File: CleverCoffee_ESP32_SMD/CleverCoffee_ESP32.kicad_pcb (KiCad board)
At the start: 2 copper layers, 51.5 x 81.8 mm, 48 parts, among them Q1 2N7002, Q2 2N7002, Q3 2N7002, Q4 2N7002, Q5 2N7002

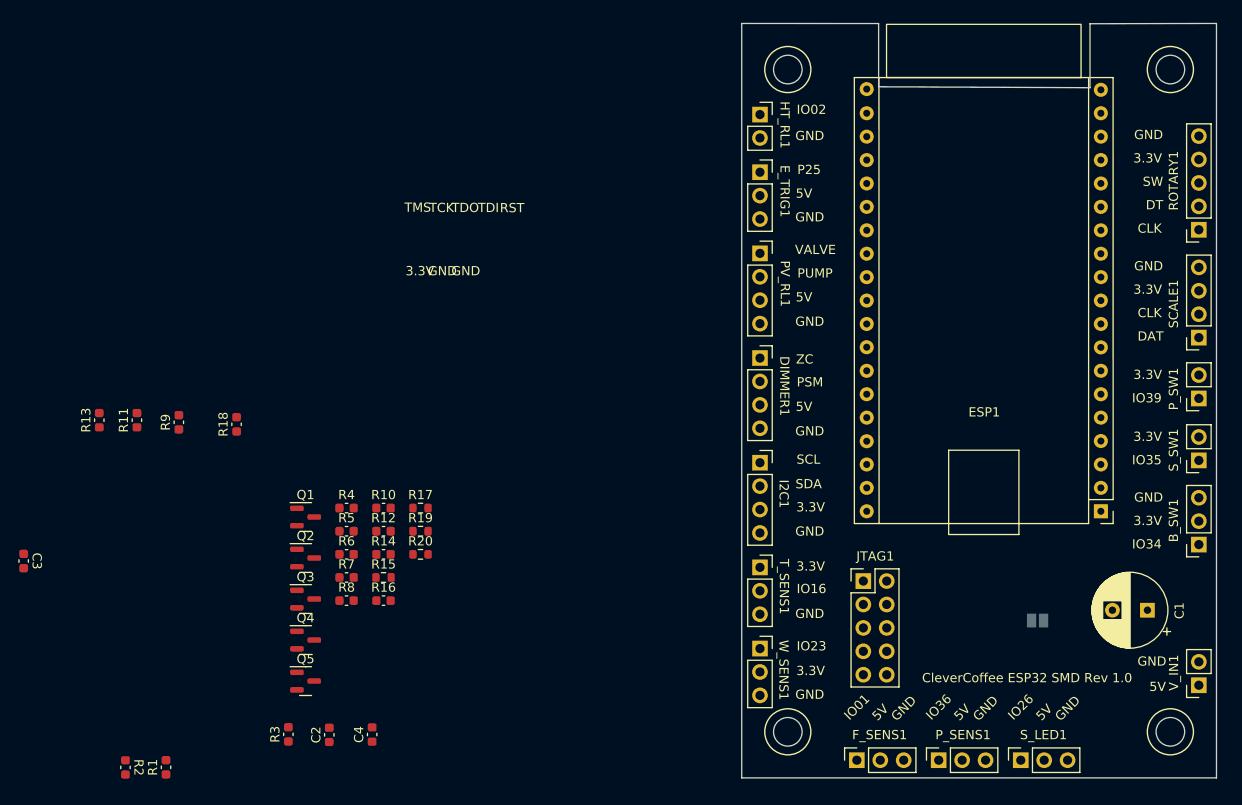
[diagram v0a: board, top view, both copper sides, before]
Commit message: Finishes SMD version for production
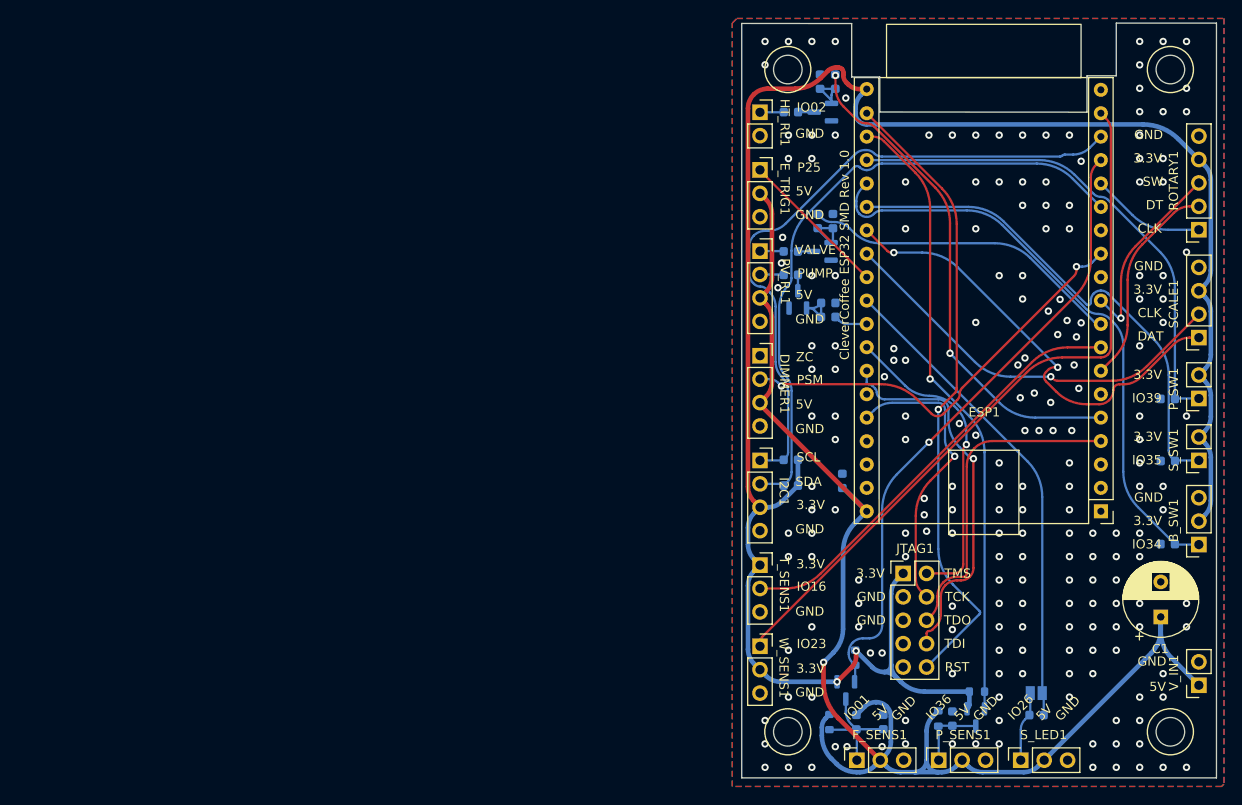
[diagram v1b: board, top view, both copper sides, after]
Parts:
- C2, C3, C4, Q1, Q2, Q3, Q4, Q5, R1, R10, R11, R12, R13, R14, R15, R16, R17, R18, R19, R2, R20, R3, R4, R5, R6, R7, R8, R9: moved to B.Cu
- moved R13 115.9 mm to (163.1, 89.3), turned to 0 degrees
- moved R11 112.6 mm to (163.1, 105.0), turned to 0 degrees
- moved R9 107.4 mm to (163.1, 96.0), turned to 0 degrees
- moved R18 92.3 mm to (148.8, 123.6), turned to 0 degrees
- moved C3 89.2 mm to (127.8, 98.2), turned to 90 degrees
- moved R2 79.5 mm to (122.2, 95.9), turned to 0 degrees
- moved Q3 77.1 mm to (125.7, 58.2), turned to 180 degrees
- moved R1 74.3 mm to (122.2, 98.7), turned to 0 degrees
- moved Q5 72.8 mm to (142.2, 123.8), turned to -90 degrees
- moved R14 70.9 mm to (127.0, 54.9), turned to -90 degrees
- moved R16 69.0 mm to (122.2, 58.2), turned to 180 degrees
- moved R12 68.0 mm to (125.3, 54.9), turned to 90 degrees
- moved Q2 65.2 mm to (125.6, 73.3), turned to 180 degrees
- moved R7 64.1 mm to (125.1, 70.0), turned to -90 degrees
- moved C4 63.0 mm to (139.7, 124.0), turned to -90 degrees
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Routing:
- net +3V3: track 0.00 -> 212.3 mm, vias 0 -> 2
- net +5V: track 0.00 -> 155.2 mm, vias 0 -> 1
- net IO23: track 0.00 -> 77.6 mm
- net SCL: track 0.00 -> 71.1 mm
- net SDA: track 0.00 -> 69.4 mm
- net RST: track 0.00 -> 68.7 mm, vias 0 -> 1
- net IO1: track 0.00 -> 68.4 mm, vias 0 -> 1
- net IO36: track 0.00 -> 67.7 mm, vias 0 -> 1
- net IO34: track 0.00 -> 65.2 mm
- net IO35: track 0.00 -> 54.8 mm
- net IO39: track 0.00 -> 54.5 mm
- net IO2: track 0.00 -> 54.4 mm, vias 0 -> 2
- net IO26: track 0.00 -> 52.6 mm
- net SC_DAT: track 0.00 -> 49.6 mm, vias 0 -> 2
- net IO16: track 0.00 -> 47.3 mm
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- added copper zone on B.Cu, net GND
- added copper zone on F.Cu, net GND
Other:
- board size 51.5 x 81.8 mm -> 51.5 x 81.9 mm
- board text added: "{ "ViaStitching": "0.2", "stitch_zone_0": { "HSpacing": "2.54", "VSpacing": "2.54", "Clearance": "0", "Randomize": false } }"

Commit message: Finalize DRC and add production files
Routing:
- net ZC: track 0.00 -> 51.8 mm, vias 0 -> 2
- net GND: track 0.00 -> 5.48 mm, vias 205 -> 246
- net TDI: track 41.0 -> 44.3 mm
- net SCL: track 71.1 -> 72.8 mm
- net SDA: track 69.4 -> 70.9 mm
- net PSM: track 46.4 -> 47.7 mm
- net +5V: track 155.2 -> 154.3 mm
- net +3V3: track 212.3 -> 211.8 mm
- net (no net): vias 1 -> 0
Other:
- outline, holes or cut-outs redrawn
